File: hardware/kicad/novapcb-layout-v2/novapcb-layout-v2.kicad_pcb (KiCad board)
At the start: 6 copper layers, 80 x 60 mm, 83 parts, among them J1 USB-C_2.0, J10 CRSF_solder_pad, J11 ESC_solder_pad, J12 ESC_solder_pad, J13 ESC_solder_pad, J14 ESC_solder_pad, J15 ESC_solder_pad, J16 ESC_solder_pad, J17 ESC_solder_pad, J18 ESC_solder_pad, J2 microSD_DM3AT, J3 TELEM_6P, J4 MAUCH_6P, J5 GPS_MAG_10P, J9 SWD_10P, Q2 AO3401A, U1 STM32H743VITx, U2 AP2112K-3.3, U3 ICM-42688-P_LGA-14_2.5x3mm_P0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, U4 DPS310, U5 USBLC6-2P6, U6 TPS25940A, Y1 8MHz

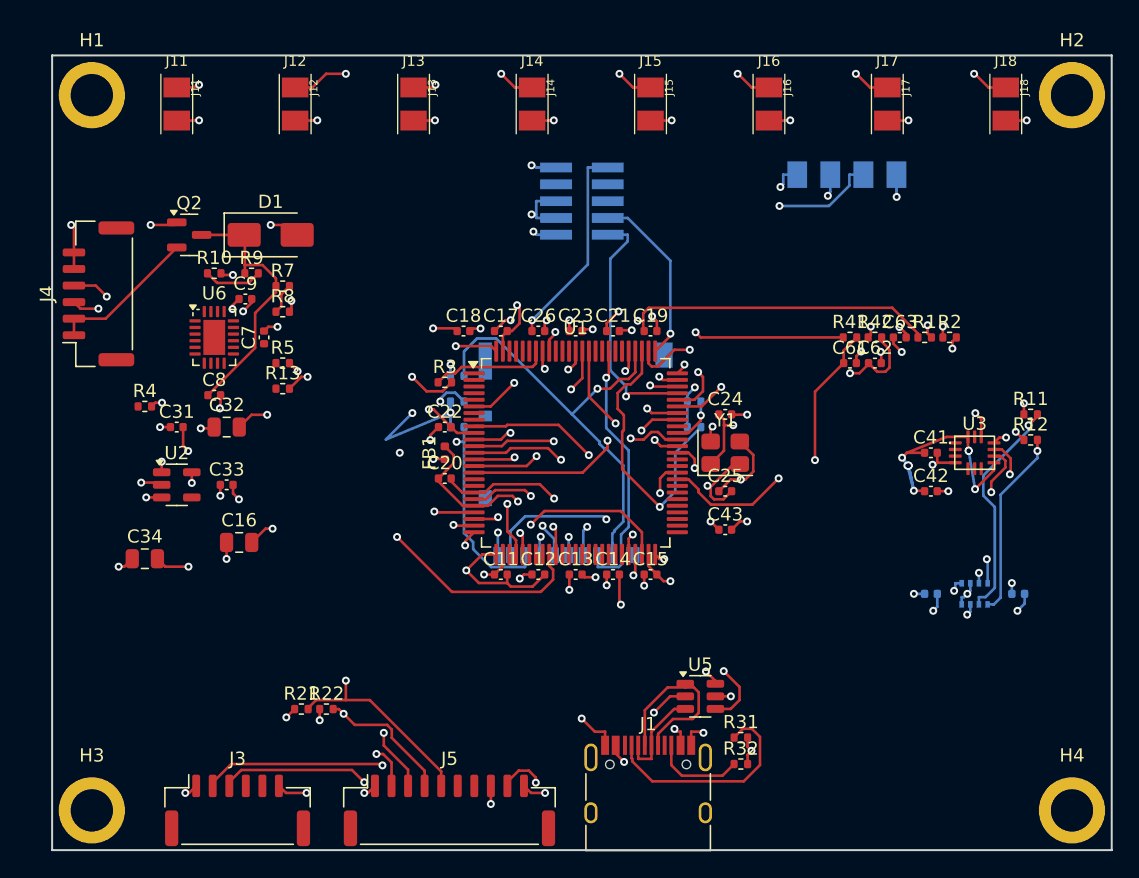
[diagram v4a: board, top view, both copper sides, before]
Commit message: Step 6 precursor: pristine 2-layer Freerouting WORKED; plane stitching + USB rework pending
Per master 2026-05-21 directive (5 Freerouting layer-constraint variants
all hung), tried the truly-pristine 2-layer DSN: ALL signal+plane tracks
stripped, plane nets entirely removed from DSN structure (layer decls +
plane decls + class membership + (net ...) blocks), inner-layer shapes
stripped from padstacks. Result: Freerouting completed in 2.8 min, 10
passes, final score 992.13, 0 unrouted on signal nets, 0 inner-layer
signal misroutes.

run_pristine_2layer.py — drives the pristine DSN + Freerouting run.
run_reroute_corrected.py — chronicle of the 5 failed Freerouting
  variants (split-class / use_layer / type=power / type=power+via-shrink
  / omit-inner-layers-from-DSN with leftover wiring). Kept as evidence
  for the Freerouting v2.2.4 layer-config pathology.
run_stitch_plane_nets.py — collision-aware plane-net stitcher; places
  through-vias offset from plane-net pads with stub trace; 113 of 141
  stitched, 35 DRC errors remaining (clearance, tracks_crossing, etc.).

Current state:
  signal routing: 629 tracks + 70 vias on F.Cu/B.Cu only, 0 misroutes
  plane stitching: 113/141 pads stitched, 35 DRC errors residual
  USB diff pair: routed F.Cu + B.Cu with 2 vias each (master directive
    requires F.Cu only, hand-routed length-matched W=0.30/S=0.10)

NOT committed-as-final: this is a precursor snapshot to discuss with
master before iterating further on stitcher refinement vs USB hand-route
vs accepting residuals as flagged.

Co-Authored-By: Claude Opus 4.7 <noreply@anthropic.com>
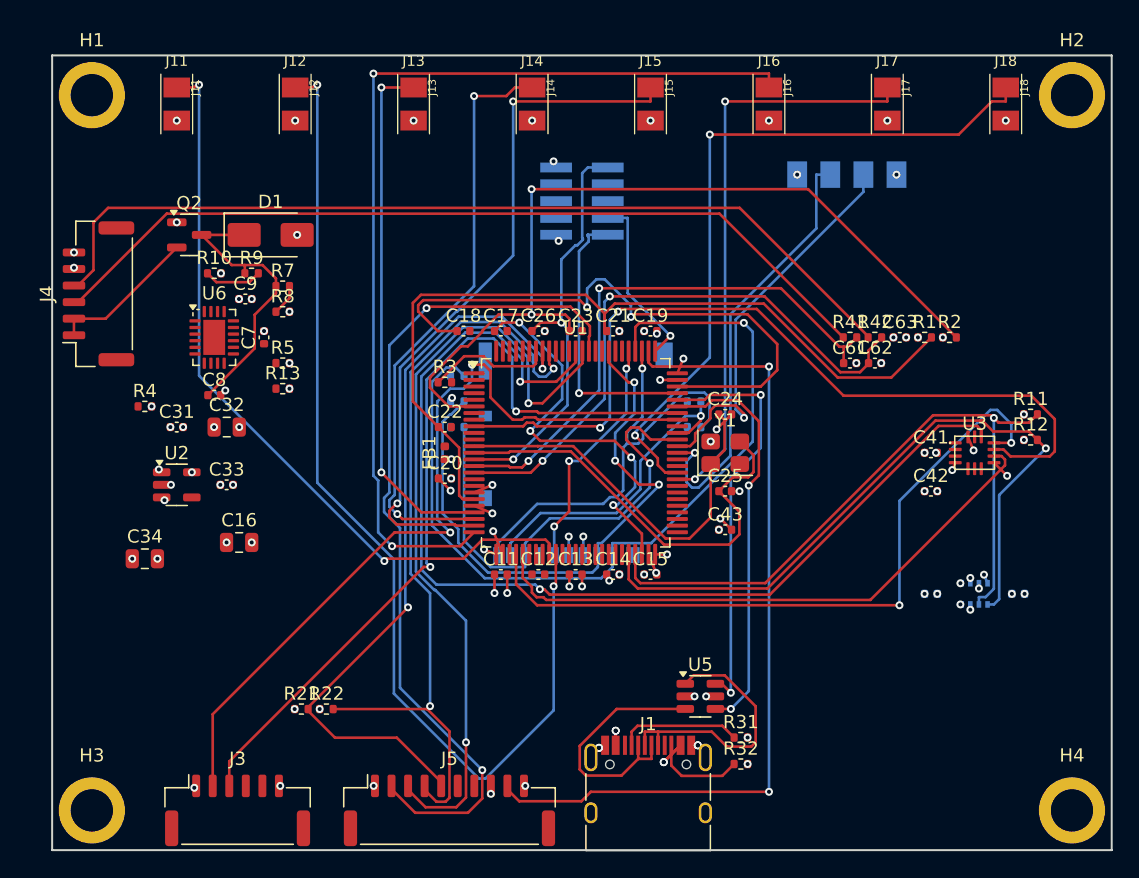
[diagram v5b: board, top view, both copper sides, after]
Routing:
- net GND: track 132.0 -> 19.2 mm, vias 61 -> 62
- net +3V3: track 71.1 -> 13.5 mm, vias 41 -> 32
- net +3V3A: track 52.0 -> 2.80 mm, vias 2 -> 4
- net SPI1_MOSI: track 35.8 -> 80.8 mm
- net SDMMC1_D3: track 33.1 -> 64.5 mm
- net MOT2: track 50.7 -> 78.8 mm, vias 3 -> 2
- net MOT6: track 48.2 -> 73.8 mm
- net GPS1_TX: track 41.9 -> 64.6 mm
- net VBAT: track 41.8 -> 64.5 mm, vias 3 -> 2
- net VCAP2: track 23.8 -> 45.9 mm
- net GPS1_RX: track 39.8 -> 59.7 mm
- net IMU1_CS: track 44.8 -> 63.0 mm
- net BUZZER: track 45.7 -> 62.9 mm
- net USART1_TX: track 50.1 -> 62.3 mm
- net USBC_D_M_PRE: track 7.34 -> 19.1 mm
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
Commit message: Step 6 precursor: R1-amended stitcher — 0 DRC errors, 102/130 stitched, 28 residuals
Per master 2026-05-21 directive chain (5 Freerouting layer-constraint
variants → pristine 2-layer recipe approved → R1-amended stitching
with at-pad + short-fanout-stub + rip-reroute):

Current state:
  pristine 2-layer Freerouting: 629 signal tracks + 70 signal vias on
    F.Cu/B.Cu only; 0 inner-layer misroutes; 2.8 min runtime.
  USB: FR pristine route on F.Cu+B.Cu (2 vias/line); impedance contract
    met (94.4Ω throughout per symmetric JLC06161H-7628 stackup).
    Per master: 6b SI sim is the formal verdict (not by-eye polish).
  Plane stitching: R1-amended — small via 0.40/0.30 at-pad first; if
    conflict, short fanout stub <=1mm; if still no clear spot, flag.
    Conflict-check uses proper rectangle distance (not max-dim radius).
    Result: 69 at-pad + 33 short-stub = 102 stitched cleanly.
    Residuals: 28 pads (mostly U1 LQFP-100 dense-pitch area + a few
    capacitor pads near signal-traffic regions).

Final DRC: 0 errors, 31 unconnected (28 residuals + 3 stragglers).

Iteration history (preserved for audit):
  run_pristine_2layer.py     — proven 2-layer FR recipe
  run_vias_first_reroute.py  — vias-first attempt (hung FR)
  run_usb_handroute_v2.py    — USB hand-route iterations (whack-a-mole,
                                halted per master 2026-05-21)
  run_stitch_smart.py        — earlier stitcher (at-pad-only)
  run_stitch_plane_nets.py   — earliest stitcher (2mm radius offset)
  _step1_strip.py            — split-subprocess helper for SWIG quirk
  _step2_place_vias.py       — split-subprocess helper
  _add_gnd_stitches.py       — USB GND stitch attempt
  run_usb_handroute.py       — F.Cu-only USB hand-route (rejected)
  run_stitch_r1_amended.py   — CURRENT stitcher with R1 amended fallback

Holding for master adjudication on the 28 residuals (rip-reroute vs
fine-grid+vision vs accept-and-move-on).

Co-Authored-By: Claude Opus 4.7 <noreply@anthropic.com>
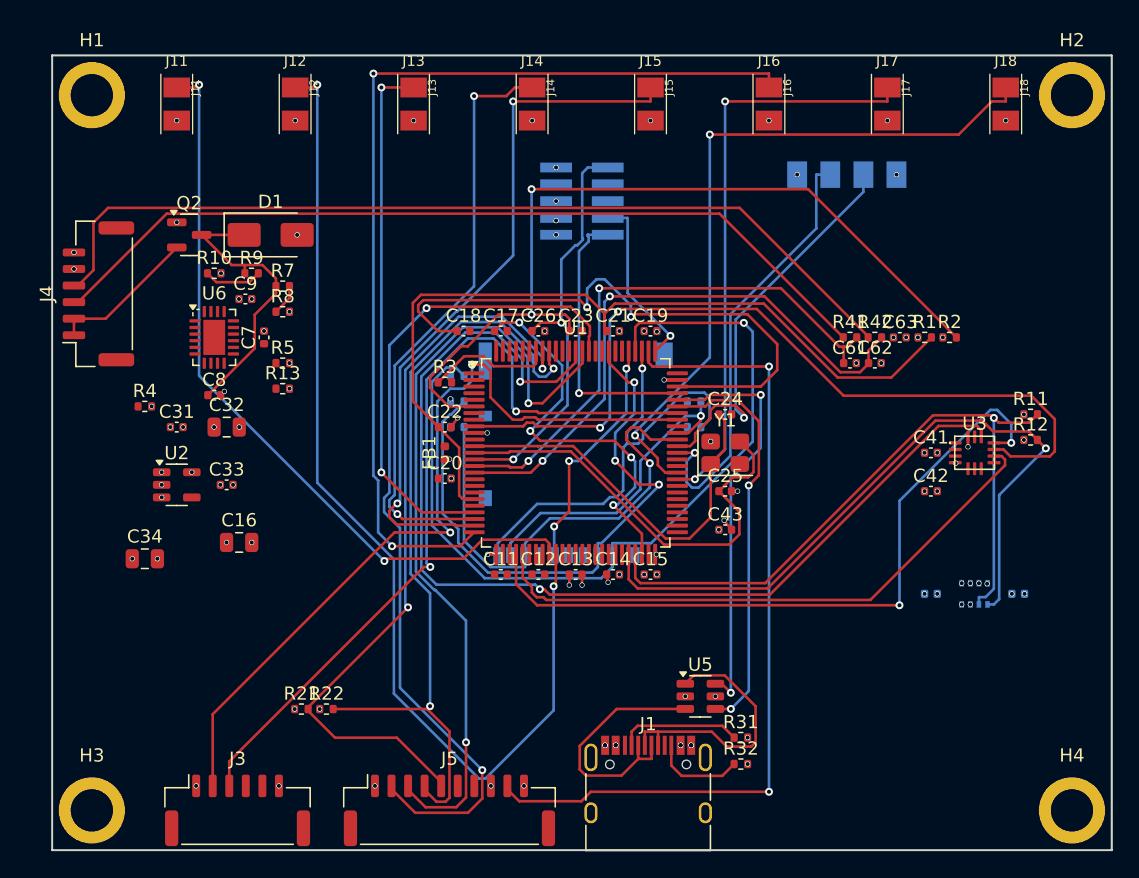
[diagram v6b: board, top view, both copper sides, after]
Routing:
- net GND: track 19.2 -> 6.40 mm
- net +3V3: track 13.5 -> 2.80 mm, vias 32 -> 27
- net +5V: track 7.40 -> 0.00 mm
- net +3V3A: track 2.80 -> 0.00 mm, vias 4 -> 2

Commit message: JLCPCB DFM ruleset alignment — tighten project rules + resize plane-stitch vias
Per Sai 2026-05-21 ("manufacturable by JLCPCB, follow ALL rules") +
master broadened audit:

docs/JLCPCB_MANUFACTURABILITY.md — comprehensive audit covering 17
rules: trace/space, drill/hole, via diameter, annular ring, hole-to-
hole, silk, mask, via-in-pad, stackup, controlled-impedance ordering.

Source: agausmann/jlcpcb-kicad-drc community KiCad DRC file (cites
JLCPCB Capabilities directly). Saved to hardware/kicad/novapcb-layout-v2/
jlcpcb.kicad_dru for custom-rules loading. WebFetch could not retrieve
JLC's JS-rendered tables; community DRC matches the verifiable JLC
impedance-page values (min trace 3.5 mil, min via 0.2 mm, min annular
0.13 mm).

Project rules tightened:
  min_hole_to_hole:        0.25 -> 0.50 mm  (JLC different-net std)
  min_via_diameter:        0.40 -> 0.46 mm  (paired with 0.20 drill)
  min_via_annular_width:   0.05 -> 0.13 mm  (JLC standard 5 mil)
  min_through_hole_diameter: 0.30 -> 0.20 mm (JLC standard now)
  min_silk_clearance:      0    -> 0.15 mm  (silk-to-pad)
  solder_mask_to_copper:   0    -> 0.10 mm

Vias resized: 102 plane-stitch vias from 0.40/0.30 (annular 0.05) to
0.46/0.20 (annular 0.13) — matches JLC standard. Freerouting signal
vias at 0.60/0.30 already meet annular 0.15.

Corrected-DRC violations surfaced (130 total):
  49 silk_overlap          — silkscreen text over pads
  31 unconnected_items     — 28 plane-stitch residuals + 3 stragglers
                              (unchanged from pre-correction)
  25 silk_over_copper      — silkscreen text drawn over copper
  20 clearance             — primarily from at-pad via clearance
                              rules now tighter (per #17 via-in-pad)
  12 text_height           — silkscreen text < 0.13 mm
  12 silk_edge_clearance   — silkscreen too close to board edge
   4 via_dangling          — orphan vias (likely zone-fill artifacts)
   4 lib_footprint_mismatch — board fp vs library fp delta (cosm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
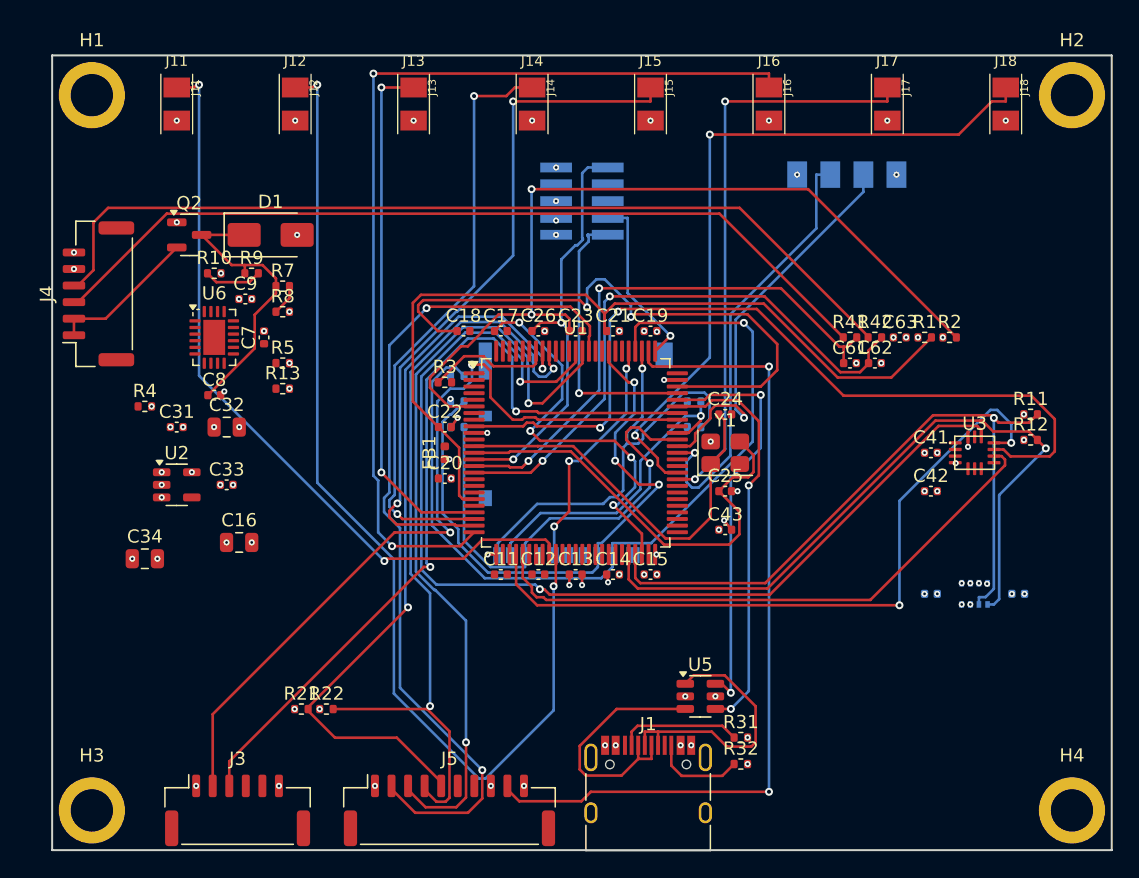
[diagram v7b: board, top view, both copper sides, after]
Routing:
- net GND: vias 62 -> 60
- net +5V: vias 15 -> 13

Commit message: JLC re-stitch: strict via-outside-pad rule, 96 placed, 38 flagged for vision
Per master 2026-05-21: NO via-in-pad anywhere (JLC standard process
forbids; wicks solder). Coordinated re-stitch:

Workflow:
  1. Strip all 102 plane-stitch vias + 18 short-stub traces (clean slate
     for plane stitching, FR signal route untouched).
  2. For each plane-net SMD pad on outer layer (130 total): find clear
     via spot at radial distance >= max(pad_half_extent, 0) + via_outer/2
     + 0.10mm mask sliver. Spiral search up to 1.0mm.
  3. Place via (0.46/0.20 JLC standard) + short stub trace from pad to via.
  4. Same-net via-to-pad check: via NOT inside SMD pad, AND solder mask
     sliver >= 0.10mm to pad edge.

Result: 96 placed cleanly (with mask sliver). 38 flagged for vision
(no clear spot within 1.0mm — primarily under U1 LQFP-100 pin grid + a
few caps near signal traffic + J1 USB-C reversibility dupes + USB-pair
sensitive area).

DRC --severity-error: 12 errors (4 hole_to_hole still — the U3-area
caps; 4 clearance from new placements; 3 mask_bridge; 2 tracks_crossing;
2 shorting +3V3↔GND; 1 keepout area). Plus 36 unconnected items (38
flagged + 3 stragglers - some flagged shared coords).

Full --severity-all: 120 violations (down from 130 pre-restitch):
  49 silk_overlap, 36 unconnected, 25 silk_over_copper, 12 text_height,
  12 silk_edge_clearance, 4 lib_footprint_mismatch, 4 hole_to_hole,
  4 clearance, 3 solder_mask_bridge, 2 via_dangling, 2 tracks_crossing,
  2 shorting_items, 1 items_not_allowed.

Remaining work (in parallel per master):
  - Re-render vision sheets for the 38 flagged pads
  - Fix 4 U3-area hole_to_hole via zigzag
  - Investigate + fix 4 lib_footprint_mismatch
  - Silk/mask global cleanup (98 silkscreen items)
  - Resolve the 14 placement-induced errors (some may be addressed
    by the vision loop's repositioning)
  - via_dangling 2 (likely zone-refill artifacts)

Co-Authored-By: Claude Opus 4.7 <noreply@anthropic.com>
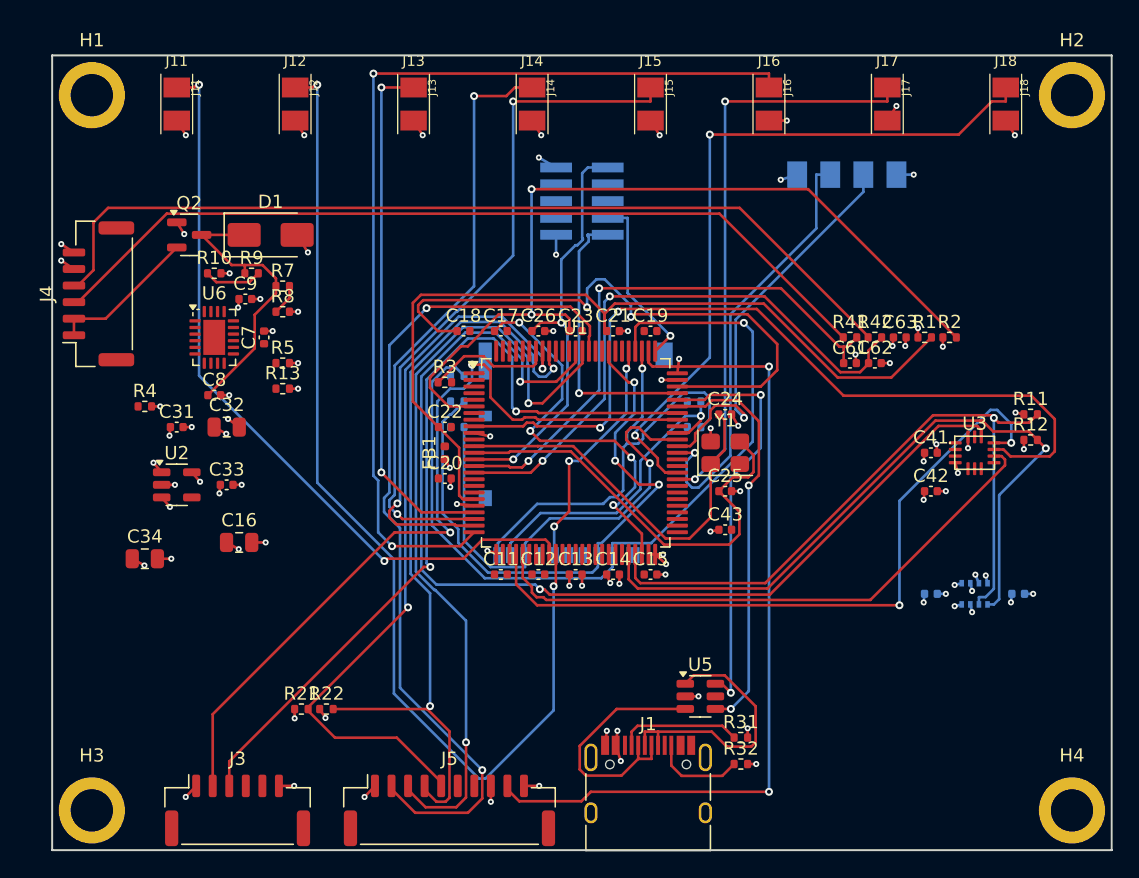
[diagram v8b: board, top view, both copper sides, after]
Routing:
- net GND: track 6.40 -> 50.7 mm, vias 60 -> 55
- net +3V3: track 2.80 -> 22.2 mm
- net +5V: track 0.00 -> 11.5 mm, vias 13 -> 12
- net +3V3A: track 0.00 -> 2.00 mm
